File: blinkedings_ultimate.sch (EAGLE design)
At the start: 26 parts, among them IC1 FT232RL, T1 BC807-16, T4 BC847, T5 BC847, T6 BC847

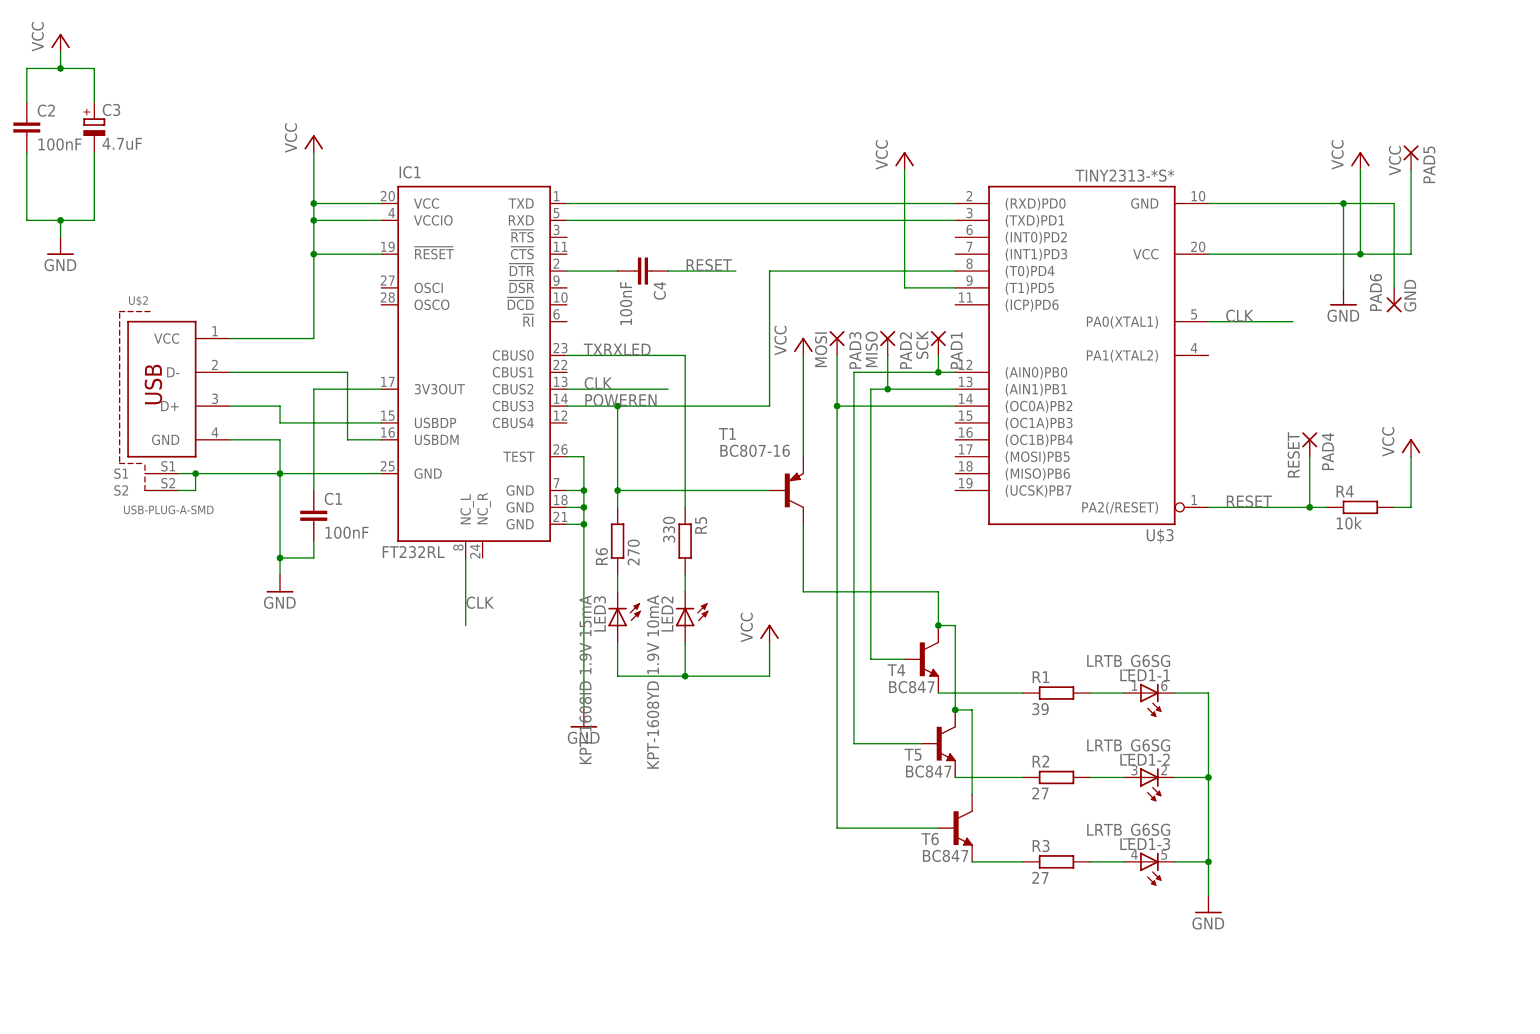
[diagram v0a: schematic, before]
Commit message: move led to emitter circuit, add appropriate base resitors
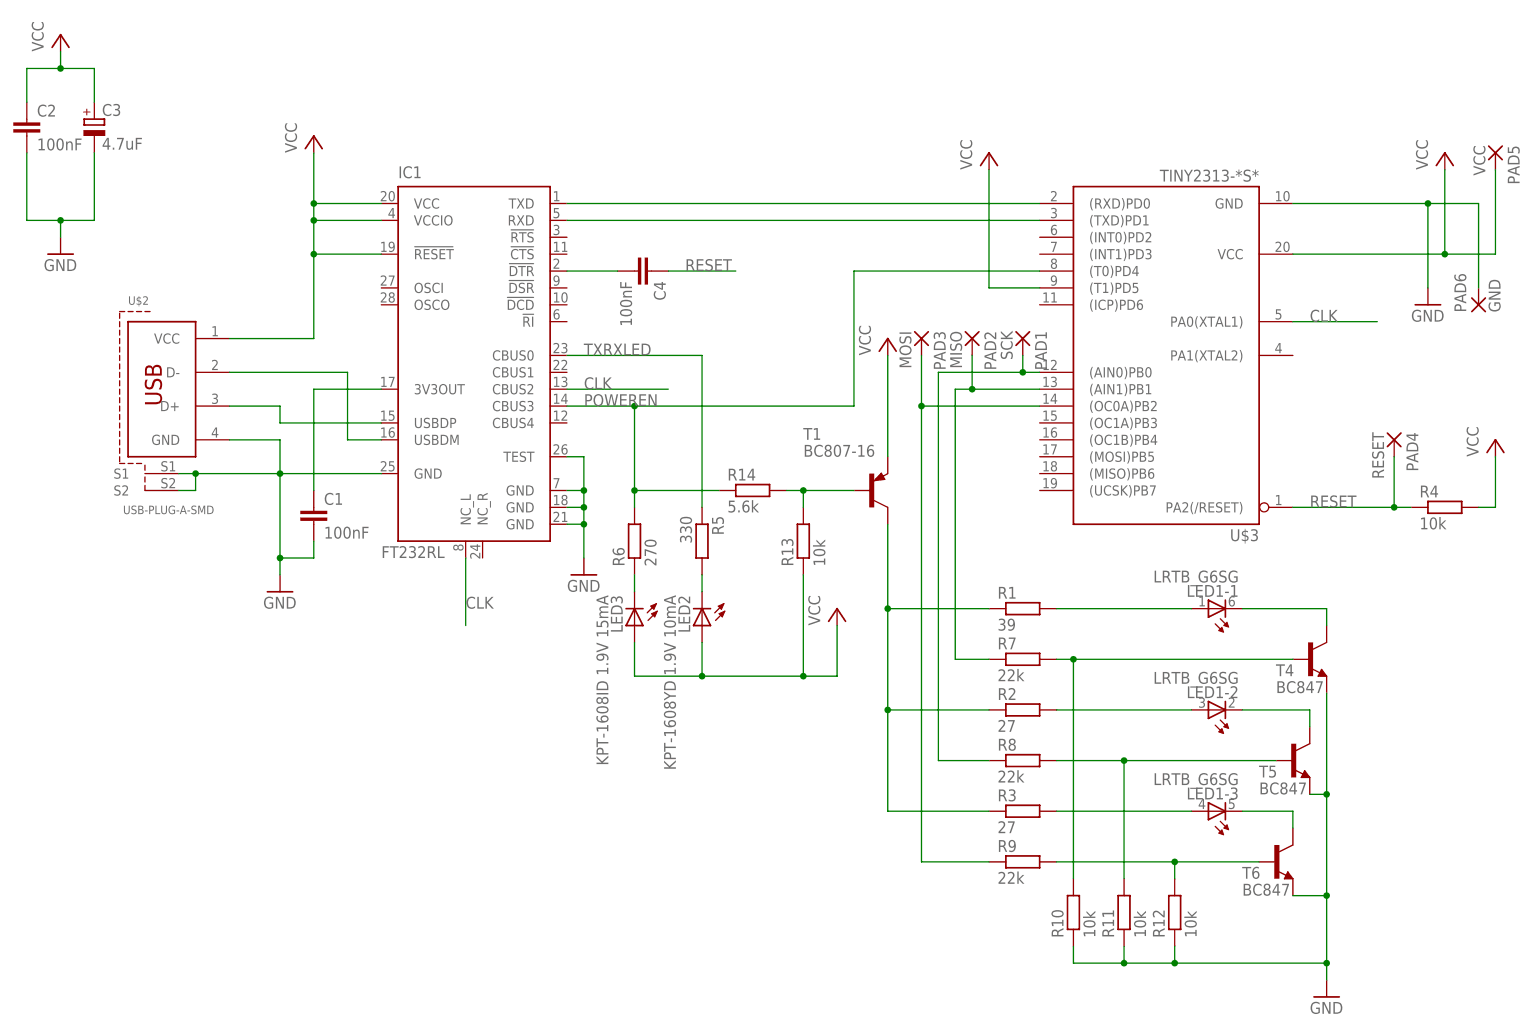
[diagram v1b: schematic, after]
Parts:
- added R10, R11, R12, R13: 10k, resistor:R-EU_R0603
- added R14: 5.6k, resistor:R-EU_R0603
- added R7, R8, R9: 22k, resistor:R-EU_R0603
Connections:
- removed net N$22: R1.1, T4.E
- new net N$12: R12.2, R9.2, T6.B
- new net N$13: R11.2, R8.2, T5.B
- new net N$17: R10.2, R7.2, T4.B
- new net N$18: LED1-2.C, T5.C
- new net N$19: R1.1, R2.1, R3.1, T1.C
- net GND: now also R10.1, R11.1, R12.1, T4.E, T5.E, T6.E; no longer LED1-1.C, LED1-2.C, LED1-3.C
- net N$14: now also R7.1; no longer T4.B
- net N$15: now also R8.1; no longer T5.B
- net N$16: now also R9.1; no longer T6.B
- net N$20: now also LED1-3.C, T6.C; no longer R3.1, T6.E
- net N$21: now also R13.2, R14.2, T1.B; no longer R2.1, T5.E
- net N$8: now also LED1-1.C; no longer T1.C, T5.C, T6.C
- net POWEREN: now also R14.1; no longer T1.B
- net VCC: now also R13.1
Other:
- moved on the sheet: LED1-1, LED1-2, LED1-3, LED2, LED3, PAD1, PAD2, PAD3, PAD4, PAD5, PAD6, R1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

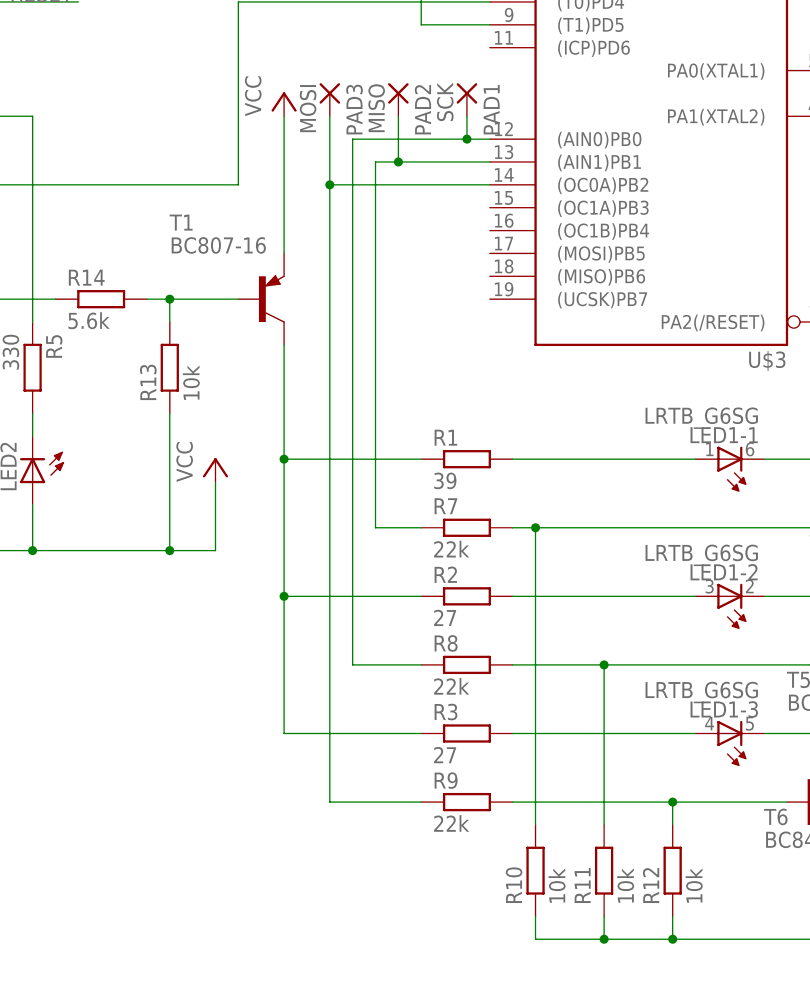
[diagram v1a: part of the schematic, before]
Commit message: 27k base resistors for blue and green
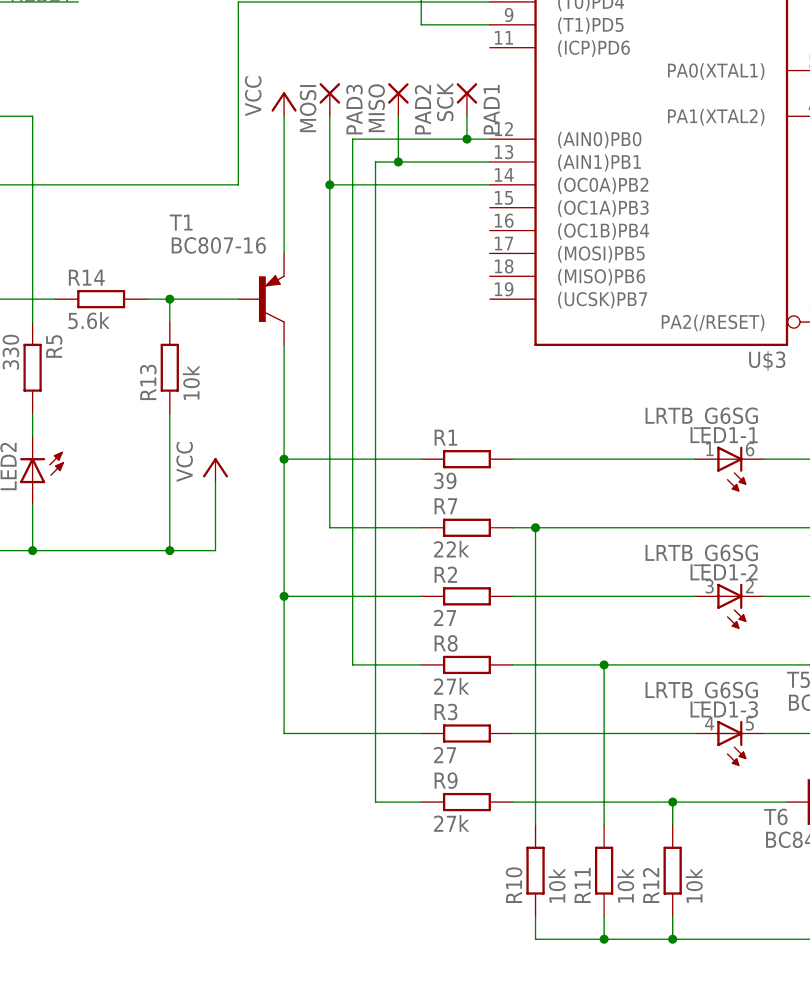
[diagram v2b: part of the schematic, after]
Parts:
- R8, R9: value 22k -> 27k
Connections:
- net N$14: now also R9.1; no longer R7.1
- net N$16: now also R7.1; no longer R9.1
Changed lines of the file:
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@@
 <part name="T1" library="transistor" deviceset="*-PNP-" device="SOT23-BEC" technology="BC857C" value="BC807-16"/>
 <part name="R7" library="resistor" deviceset="R-EU_" device="R0603" value="22k"/>
-<part name="R8" library="resistor" deviceset="R-EU_" device="R0603" value="22k"/>
-<part name="R9" library="resistor" deviceset="R-EU_" device="R0603" value="22k"/>
+<part name="R8" library="resistor" deviceset="R-EU_" device="R0603" value="27k"/>
+<part name="R9" library="resistor" deviceset="R-EU_" device="R0603" value="27k"/>
 <part name="R10" library="resistor" deviceset="R-EU_" device="R0603" value="10k"/>
 <part name="R11" library="resistor" deviceset="R-EU_" device="R0603" value="10k"/>
@@
 <net name="N$14" class="0">
 <segment>
-<wire x1="142.24" y1="-7.62" x2="142.24" y2="33.02" width="0.1524" layer="91"/>
+<wire x1="142.24" y1="-38.1" x2="142.24" y2="33.02" width="0.1524" layer="91"/>
 <pinref part="U$3" gate="G$1" pin="(AIN1)PB1"/>
 <wire x1="142.24" y1="33.02" x2="144.78" y2="33.02" width="0.1524" layer="91"/>
@@
 <wire x1="144.78" y1="38.1" x2="144.78" y2="33.02" width="0.1524" layer="91"/>
 <junction x="144.78" y="33.02"/>
-<pinref part="R7" gate="G$1" pin="1"/>
-<wire x1="142.24" y1="-7.62" x2="147.32" y2="-7.62" width="0.1524" layer="91"/>
+<pinref part="R9" gate="G$1" pin="1"/>
+<wire x1="142.24" y1="-38.1" x2="147.32" y2="-38.1" width="0.1524" layer="91"/>
 </segment>
 </net>
@@
 <net name="N$16" class="0">
 <segment>
-<wire x1="137.16" y1="30.48" x2="137.16" y2="-38.1" width="0.1524" layer="91"/>
+<wire x1="137.16" y1="30.48" x2="137.16" y2="-7.62" width="0.1524" layer="91"/>
 <pinref part="U$3" gate="G$1" pin="(OC0A)PB2"/>
 <wire x1="137.16" y1="30.48" x2="154.94" y2="30.48" width="0.1524" layer="91"/>
@@
 <wire x1="137.16" y1="38.1" x2="137.16" y2="30.48" width="0.1524" layer="91"/>
 <junction x="137.16" y="30.48"/>
-<pinref part="R9" gate="G$1" pin="1"/>
-<wire x1="137.16" y1="-38.1" x2="147.32" y2="-38.1" width="0.1524" layer="91"/>
-</segment>
-</net>
+<pinref part="R7" gate="G$1" pin="1"/>
+<wire x1="147.32" y1="-7.62" x2="137.16" y2="-7.62" width="0.1524" layer="91"/>
+</segment>
+</net>

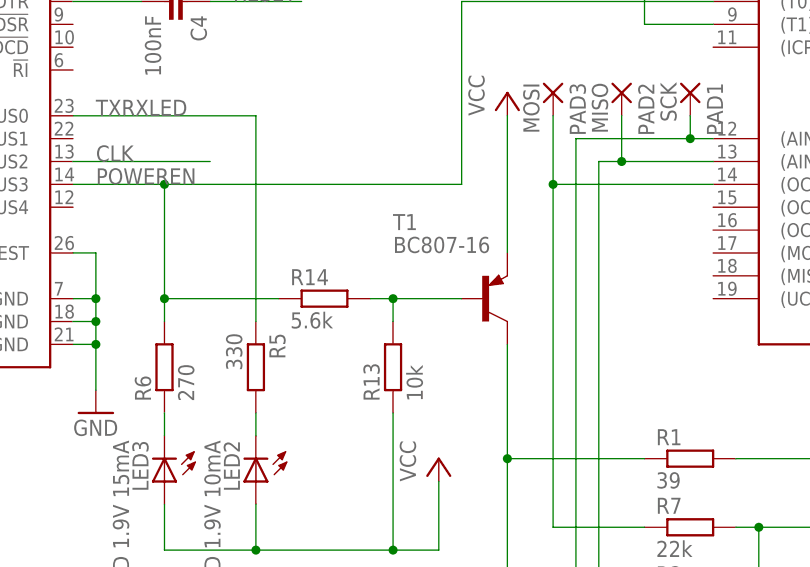
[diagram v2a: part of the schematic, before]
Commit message: BC807-16 -> BC807-40
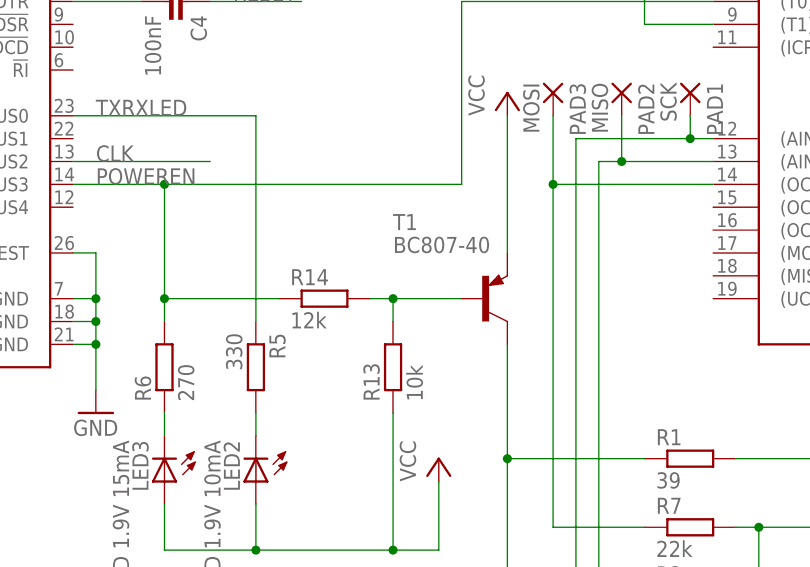
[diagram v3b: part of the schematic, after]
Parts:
- R14: value 5.6k -> 12k
- T1: value BC807-16 -> BC807-40
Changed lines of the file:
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@@
 <part name="P+6" library="supply1" deviceset="VCC" device=""/>
 <part name="P+7" library="supply1" deviceset="VCC" device=""/>
-<part name="T1" library="transistor" deviceset="*-PNP-" device="SOT23-BEC" technology="BC857C" value="BC807-16"/>
+<part name="T1" library="transistor" deviceset="*-PNP-" device="SOT23-BEC" technology="BC857C" value="BC807-40"/>
 <part name="R7" library="resistor" deviceset="R-EU_" device="R0603" value="22k"/>
 <part name="R8" library="resistor" deviceset="R-EU_" device="R0603" value="27k"/>
@@
 <part name="GND6" library="supply1" deviceset="GND" device=""/>
 <part name="R13" library="resistor" deviceset="R-EU_" device="R0603" value="10k"/>
-<part name="R14" library="resistor" deviceset="R-EU_" device="R0603" value="5.6k"/>
+<part name="R14" library="resistor" deviceset="R-EU_" device="R0603" value="12k"/>
 </parts>
 <sheets>
